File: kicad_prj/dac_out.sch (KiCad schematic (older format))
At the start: 0 parts

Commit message: Schematics 5
Started isolation part.
Selected ICs for SPI isolation and general digital I/Os.
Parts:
- added C? (x2): 10uF, symbol CP
- added C? (x3): 0.1uF, symbol C
- added R?: 3.24k, symbol R
- added U?: DAC8574, symbol DAC8574
- added U?: LM4040A, symbol LM4040A
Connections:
- net labels added: +5V, CH0, CH1, CH2, CH3, CH[0..3], GND, GNDA, GNDD, OUT, SCL, SDA, VDD
- wire segments 0 -> 49

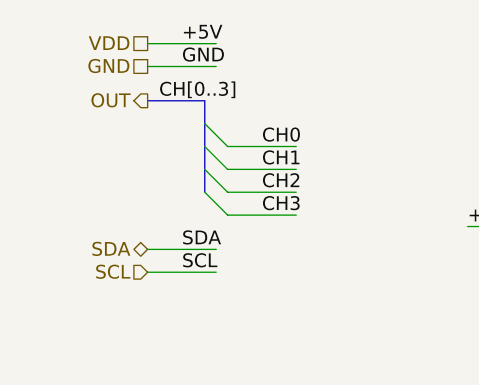
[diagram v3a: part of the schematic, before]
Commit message: Schematics 10
All power isolated part is wired.
Started control part.
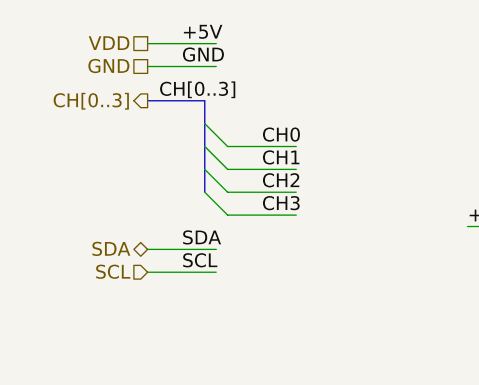
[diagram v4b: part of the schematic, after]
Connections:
- net labels removed: OUT
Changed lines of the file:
@@
 $Descr A 11000 8500
 encoding utf-8
-Sheet 8 11
+Sheet 8 13
 Title ""
 Date ""
@@
 $EndComp
 $Comp
-L GNDD #PWR?
+L GNDD #PWR068
 U 1 1 5657B004
 P 5500 4750
-F 0 "#PWR?" H 5500 4500 50  0001 C CNN
+F 0 "#PWR068" H 5500 4500 50  0001 C CNN
 F 1 "GNDD" H 5500 4600 50  0000 C CNN
 F 2 "" H 5500 4750 60  0000 C CNN
@@
 $EndComp
 $Comp
-L GNDD #PWR?
+L GNDD #PWR069
 U 1 1 5657B028
 P 4800 4050
-F 0 "#PWR?" H 4800 3800 50  0001 C CNN
+F 0 "#PWR069" H 4800 3800 50  0001 C CNN
 F 1 "GNDD" H 4800 3900 50  0000 C CNN
 F 2 "" H 4800 4050 60  0000 C CNN
@@
 $EndComp
 $Comp
-L GNDA #PWR?
+L GNDA #PWR070
 U 1 1 5657B042
 P 6600 3250
-F 0 "#PWR?" H 6600 3000 50  0001 C CNN
+F 0 "#PWR070" H 6600 3000 50  0001 C CNN
 F 1 "GNDA" H 6600 3100 50  0000 C CNN
 F 2 "" H 6600 3250 60  0000 C CNN
@@
 $EndComp
 $Comp
-L GNDD #PWR?
+L GNDD #PWR071
 U 1 1 5657B06C
 P 4550 4750
-F 0 "#PWR?" H 4550 4500 50  0001 C CNN
+F 0 "#PWR071" H 4550 4500 50  0001 C CNN
 F 1 "GNDD" H 4550 4600 50  0000 C CNN
 F 2 "" H 4550 4750 60  0000 C CNN
@@
 $EndComp
 $Comp
-L GNDA #PWR?
+L GNDA #PWR072
 U 1 1 5657B072
 P 6750 4750
-F 0 "#PWR?" H 6750 4500 50  0001 C CNN
+F 0 "#PWR072" H 6750 4500 50  0001 C CNN
 F 1 "GNDA" H 6750 4600 50  0000 C CNN
 F 2 "" H 6750 4750 60  0000 C CNN
@@
 $EndComp
 $Comp
-L GNDA #PWR?
+L GNDA #PWR073
 U 1 1 5657B078
 P 7200 4200
-F 0 "#PWR?" H 7200 3950 50  0001 C CNN
+F 0 "#PWR073" H 7200 3950 50  0001 C CNN
 F 1 "GNDA" H 7200 4050 50  0000 C CNN
 F 2 "" H 7200 4200 60  0000 C CNN
@@
 $EndComp
 $Comp
-L GNDA #PWR?
+L GNDA #PWR074
 U 1 1 5657BB6B
 P 4800 4750
-F 0 "#PWR?" H 4800 4500 50  0001 C CNN
+F 0 "#PWR074" H 4800 4500 50  0001 C CNN
 F 1 "GNDA" H 4800 4600 50  0000 C CNN
 F 2 "" H 4800 4750 60  0000 C CNN
@@
 GND
 Text HLabel 2900 3050 0    60   Output ~ 0
-OUT
+CH[0..3]
 Text Label 3050 2800 0    60   ~ 0
 +5V
